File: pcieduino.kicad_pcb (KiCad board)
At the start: 2 copper layers, 51 x 30 mm, 31 parts, among them IC1 ATMEGA328P-A, J1 PCIE-MINI, J2 ANALOG_POWER, J3 ISP, J4 DIGITAL, SW1 SW_PUSH, U1 MCP2200, X1 12MHZ, X2 8MHz

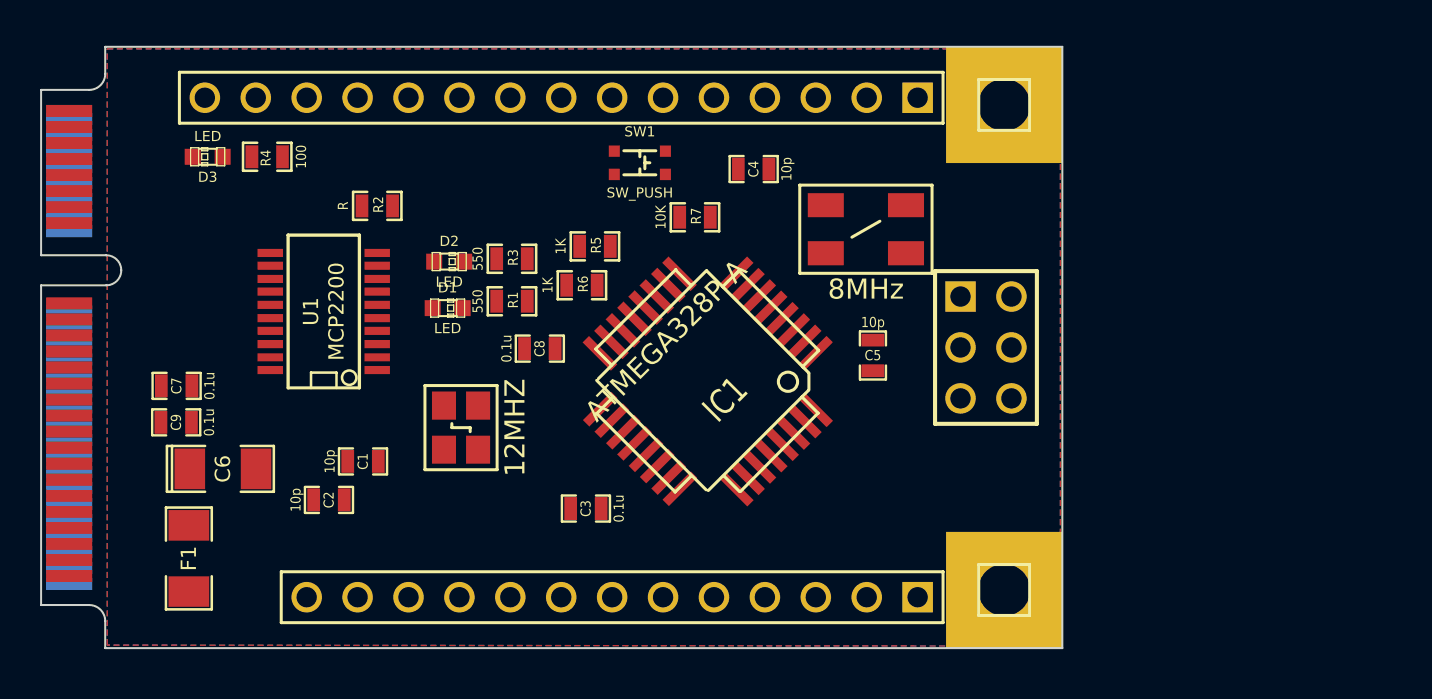
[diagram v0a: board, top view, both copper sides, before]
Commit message: work in progress: Mouser part numbers, new switch footprint, fixed footprint mixups
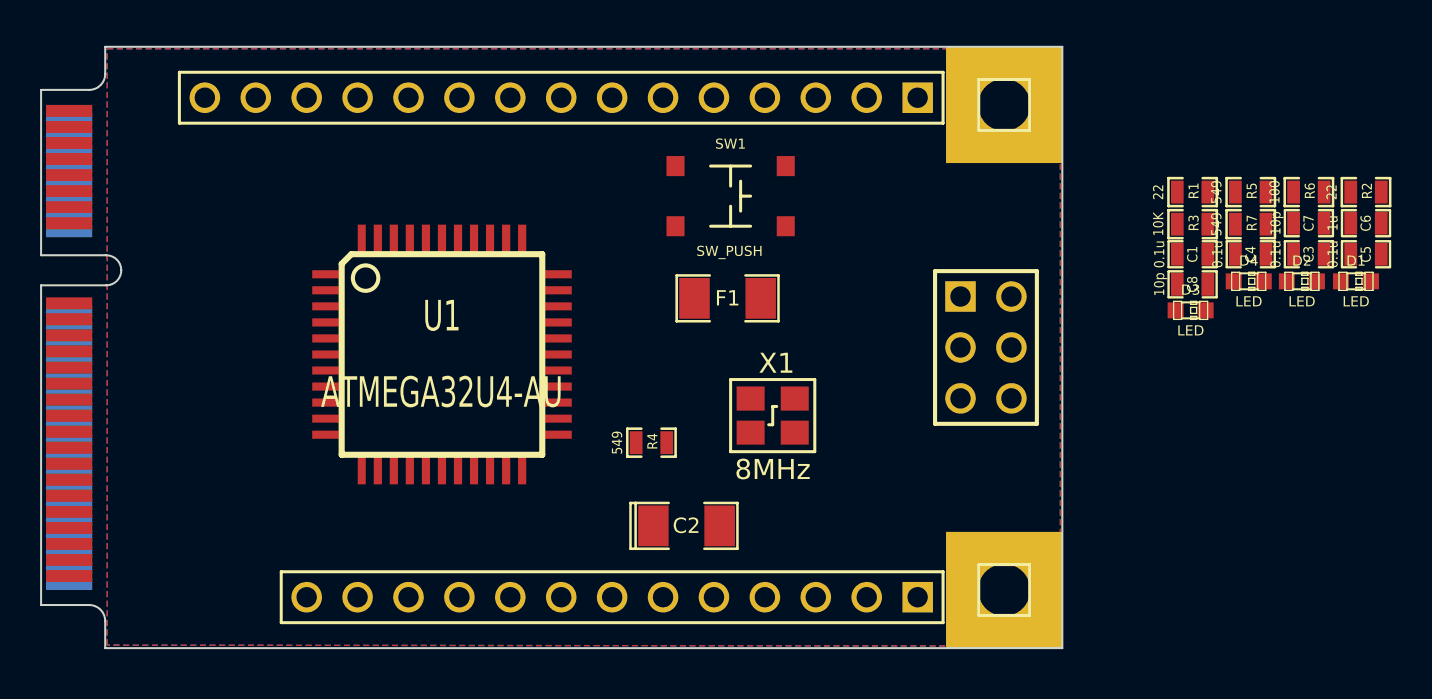
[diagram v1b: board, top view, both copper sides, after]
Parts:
- removed C9: 0.1u, SM0603_Capa
- removed IC1: ATMEGA328P-A, TQFP32
- removed X2: 8MHz, SMDXTAL_50x32
- added D4: LED, LED-0603, F.Cu at (109.3, 111.7)
- C1, C4, C5: value 10p -> 0.1u
- C2: value 10p -> 10u; footprint SM0603_Capa -> SM1206POL
- C6: value 10u -> 1u; footprint SM1206POL -> SM0603_Capa
- C7, C8: value 0.1u -> 10p
- R1: value 550 -> 22
- R2: value R -> 22
- R3: value 550 -> 10K
- R4: value 100 -> 549
- R5: value 1K -> 549
- R6: value 1K -> 100
- R7: value 10K -> 549
- U1: value MCP2200 -> ATMEGA32U4-AU; footprint SSOP20 -> TQFP44
- X1: value 12MHZ -> 8MHz
- moved C6 58.3 mm to (115.2, 108.8)
- moved C7 57.1 mm to (112.3, 108.8), turned to 0 degrees
- moved D3 49.6 mm to (106.4, 113.2), turned to 0 degrees
- moved R2 49.3 mm to (115.2, 107.2)
- moved D1 45.3 mm to (114.7, 111.7)
- moved C1 42.7 mm to (106.5, 110.3)
- moved D2 42.5 mm to (112.0, 111.7)
- moved C3 38.2 mm to (112.3, 110.3), turned to 0 degrees
- moved R6 36.6 mm to (112.3, 107.2)
- moved R1 34.4 mm to (106.5, 107.2)
- moved R3 34.0 mm to (106.5, 108.8)
- moved R5 32.8 mm to (109.4, 107.2)
- moved C8 32.7 mm to (106.5, 111.8)
- moved F1 29.8 mm to (83.3, 112.5), turned to 0 degrees
- moved R7 27.7 mm to (109.4, 108.8)
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- renumbered J3 to J2, J4 to J3, J2 to J4
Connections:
- C1 pad 1: N-0000035 -> /UVCC
- C2 pad 1: N-0000034 -> VCC
- C3 pad 1: /AREF -> VCC
- C4 pad 1: N-0000041 -> VCC
- C5 pad 1: N-0000040 -> /AREF
- C6 pad 1: VCC -> N-000006
- C7 pad 1: VCC -> N-0000019
- C8 pad 1: /RESET -> N-0000018
- C8 pad 2: /DTR -> GND
- D1 pad 1: N-0000038 -> N-0000026
- D1 pad 2: N-0000033 -> /TXLED
- D2 pad 1: N-0000037 -> N-0000027
- D2 pad 2: N-0000032 -> /RXLED
- D3 pad 1: N-0000043 -> N-0000025
- F1 pad 1: N-0000039 -> /UVCC
- J1 pad 2: N-0000039 -> /UVCC
- J1 pad 36: /USB_M -> N-000003
- J1 pad 38: /USB_P -> N-000004
- J1 pad 52: N-0000039 -> /UVCC
- J2 pad 1: /D12/MISO -> /MISO
- J2 pad 3: /D13/SCK -> /SCK
- J2 pad 4: /D11/MOSI -> /MOSI
- J3 pad 1: N-000008 -> /D0/RXI
- J3 pad 12: /D11/MOSI -> /D11
- J3 pad 13: /D12/MISO -> /D12
- J3 pad 14: /D13/SCK -> /D13
- J3 pad 2: N-000007 -> /D1/TXO
- J3 pad 3: /D2 -> /D2/SDA
- J3 pad 4: /D3 -> /D3/SCL
- J4 pad 1: /A7 -> /A5
- J4 pad 10: GND -> VCC
- J4 pad 11: GND -> VCC
- J4 pad 12: VCC -> /AREF
- J4 pad 13: VCC -> /RESET
- J4 pad 2: /A6 -> /A4
- J4 pad 3: /A5 -> /A3
- J4 pad 4: /A4 -> /A2
- J4 pad 5: /A3 -> /A1
- J4 pad 6: /A2 -> /A0
- J4 pad 7: /A1 -> /UVCC
- J4 pad 8: /A0 -> GND
- J4 pad 9: /AREF -> GND
- R1 pad 1: N-0000038 -> N-000003
- R1 pad 2: VCC -> /D-
- R2 pad 1: VCC -> /D+
- R2 pad 2: N-0000020 -> N-000004
- R3 pad 1: N-0000037 -> VCC
- R3 pad 2: VCC -> /RESET
- R4 pad 1: /D13/SCK -> N-0000026
- R4 pad 2: N-0000043 -> VCC
- R5 pad 1: /RXI -> N-0000027
- R5 pad 2: N-000008 -> VCC
- R6 pad 1: /TXO -> /D13
- R6 pad 2: N-000007 -> N-0000025
- R7 pad 1: VCC -> N-000007
- R7 pad 2: /RESET -> GND
- SW1 pad 1: /RESET -> GND
- SW1 pad 2: GND -> /RESET
- U1 pad 1: VCC -> /D7
- U1 pad 10: /RXI -> /MOSI
- U1 pad 11: /DTR -> /MISO
- U1 pad 12: /TXO -> /D11
- U1 pad 13: (no net) -> /RESET
- U1 pad 14: (no net) -> VCC
- U1 pad 15: (no net) -> GND
- U1 pad 16: (no net) -> N-0000018
- U1 pad 17: VCC -> N-0000019
- U1 pad 18: /USB_M -> /D3/SCL
- U1 pad 19: /USB_P -> /D2/SDA
- U1 pad 2: N-0000035 -> /UVCC
- U1 pad 20: GND -> /D0/RXI
- U1 pad 3: N-0000034 -> /D-
- U1 pad 4: N-0000020 -> /D+
- U1 pad 5: N-0000033 -> GND
- U1 pad 6: N-0000032 -> N-000006
- U1 pad 7: (no net) -> /UVCC
- U1 pad 8: (no net) -> /RXLED
- U1 pad 9: (no net) -> /SCK
- X1 pad 1: N-0000035 -> N-0000019
- X1 pad 2: N-0000034 -> N-0000018

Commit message: work in progress, after autorouting and all connections
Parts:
- SW1: value SW_PUSH -> RESET
- U1: value ATMEGA32U4-AU -> ATMEGA32U4
- moved R2 60.9 mm to (56.0, 121.8), turned to 180 degrees
- moved R6 52.5 mm to (59.8, 106.2), turned to 270 degrees
- moved R1 52.0 mm to (56.0, 119.8), turned to 180 degrees
- moved D3 49.2 mm to (57.7, 106.2), turned to 90 degrees
- moved C1 49.1 mm to (58.0, 117.9)
- moved D4 48.1 mm to (61.2, 110.0), turned to 90 degrees
- moved C5 46.7 mm to (69.8, 121.6), turned to 90 degrees
- moved R7 46.1 mm to (63.3, 110.1), turned to 270 degrees
- moved C3 45.5 mm to (67.0, 114.4), turned to 90 degrees
- moved C4 44.3 mm to (65.3, 114.4), turned to 90 degrees
- moved C6 34.0 mm to (83.3, 120.9), turned to 270 degrees
- moved D1 27.7 mm to (87.0, 113.8), turned to 180 degrees
- moved D2 25.2 mm to (87.0, 115.8), turned to 180 degrees
- moved R3 25.1 mm to (86.7, 124.3)
- moved C2 24.4 mm to (59.4, 113.0), turned to 180 degrees
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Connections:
- J1 pad 36: N-000003 -> N-000002
- R1 pad 1: N-000003 -> /D-
- R1 pad 2: /D- -> N-000002
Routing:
- net GND: track 0.00 -> 143.4 mm, vias 0 -> 18
- net VCC: track 0.00 -> 105.5 mm
- net /UVCC: track 0.00 -> 73.0 mm, vias 0 -> 6
- net /RESET: track 0.00 -> 59.7 mm, vias 0 -> 1
- net /D+: track 0.00 -> 30.2 mm, vias 0 -> 4
- net /D-: track 0.00 -> 30.2 mm, vias 0 -> 4
- net /A5: track 0.00 -> 25.1 mm, vias 0 -> 1
- net /D11: track 0.00 -> 24.4 mm, vias 0 -> 1
- net /A4: track 0.00 -> 21.9 mm, vias 0 -> 1
- net /D7: track 0.00 -> 21.2 mm, vias 0 -> 1
- net /D12: track 0.00 -> 20.2 mm
- net /A2: track 0.00 -> 18.9 mm, vias 0 -> 1
- net /A3: track 0.00 -> 18.9 mm, vias 0 -> 1
- net /D13: track 0.00 -> 17.8 mm
- net /A1: track 0.00 -> 17.2 mm, vias 0 -> 1
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- added copper zone on B.Cu, net GND
- removed copper zone on B.Cu, net VCC
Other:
- net class Default: via_dia 0.762 -> 0.6
- net class PCI: trace_width 0.4 -> 0.3; via_dia 0.762 -> 0.6
- net class Power: trace_width 0.4 -> 0.3; via_dia 0.889 -> 0.6; via_drill 0.635 -> 0.3048
- board text added: "CC-BY-SA 3.0"
- board text added: "PCIeDuino 32U4 v1"

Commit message: PCIeDuino32U4v1 submitted for printing at Seeed
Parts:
- added G***: LOGO, SQUARE, B.Cu at (59.8, 116.8)
- added G***: LOGO, OSHW, F.Cu at (67.8, 110.4)
- D1: value LED -> TX
- D2: value LED -> RX
- D3: value LED -> D13
- D4: value LED -> Power
- moved R7 0.18 mm to (63.2, 110.0)
- moved D4 0.14 mm to (61.1, 109.9)
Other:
- board text added: "0"
- board text added: "1"
- board text added: "10"
- board text added: "11"
- board text added: "12"
- board text added: "13"
- board text added: "2"
- board text added: "3"
- board text added: "4"
- board text added: "5"
- board text added: "6"
- board text added: "7"
- board text added: "8"
- board text added: "9"
- board text added: "Analog"
- board text added: "Aref"
- board text added: "G"
- board text added: "GND"
- board text added: "Gergely Imreh 2015 May"
- board text added: "I"
- board text added: "ISP"
- board text added: "O"
- board text added: "R"
- board text added: "S"
- board text added: "Tested"
- board text added: "V"
- board text added: "VCC"
- board text added: "Vin"

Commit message: Updated version, ready to print
* fixed XTAL footprint
* changed 10u bypass footprint
* general layout improvements
* added Moonpunch logo
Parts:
- added MOONPUNCH: LOGO, LOGO, B.Cu at (86.5, 110.9)
- C2: footprint SM1206POL -> SM0805
- D4: value Power -> PWR
- SW1: value RESET -> Reset
- X1: footprint SMDXTAL_32x25 -> SMDXTAL_50x32
- moved C4 19.2 mm to (84.2, 111.2), turned to 135 degrees
- moved D2 9.97 mm to (95.3, 121.4), turned to 90 degrees
- moved D1 9.71 mm to (95.2, 108.6), turned to 90 degrees
- moved R5 9.07 mm to (97.7, 121.3), turned to 90 degrees
- moved R4 8.70 mm to (97.7, 108.7), turned to 270 degrees
- moved C1 4.68 mm to (56.9, 113.3), turned to 90 degrees
- moved C7 4.65 mm to (87.0, 107.2), turned to 270 degrees
- moved R3 3.73 mm to (90.3, 123.5)
- moved C2 3.69 mm to (61.5, 116.0)
- moved SW1 2.71 mm to (89.8, 119.0), turned to 90 degrees
- moved F1 2.59 mm to (60.6, 113.3)
- moved C8 2.21 mm to (87.0, 111.2), turned to 270 degrees
- moved D3 1.95 mm to (59.6, 106.2)
- moved R6 1.75 mm to (61.5, 106.2)
- moved R7 1.72 mm to (61.5, 109.5)
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- renumbered G*** to OSHW, G*** to TESTED
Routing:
- net GND: track 143.4 -> 175.1 mm, vias 18 -> 17
- net /UVCC: track 73.0 -> 102.0 mm, vias 6 -> 7
- net /D7: track 21.2 -> 35.3 mm
- net /D5: track 16.2 -> 27.2 mm, vias 1 -> 0
- net /TXLED: track 13.0 -> 23.1 mm, vias 2 -> 0
- net /A2: track 18.9 -> 26.4 mm
- net /RXLED: track 7.04 -> 14.3 mm
- net /D12: track 20.2 -> 14.9 mm, vias 0 -> 1
- net N-0000018: track 7.82 -> 12.5 mm
- net /D11: track 24.4 -> 28.2 mm
- net /RESET: track 59.7 -> 56.4 mm
- net N-0000019: track 13.4 -> 10.1 mm
- net /D8: track 8.85 -> 11.4 mm, vias 0 -> 1
- net /MOSI: track 15.5 -> 17.4 mm
- net /D1/TXO: track 15.7 -> 14.0 mm, vias 0 -> 1
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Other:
- net class Power: trace_width 0.3 -> 0.4
- board text added: "RST"
